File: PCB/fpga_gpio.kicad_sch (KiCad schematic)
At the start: 6 parts, among them J8 Pin header, 2x4, J9 Pin header, 2x4, U14 TPAZ1043-04F, U15 TPAZ1043-04F, U16 TPAZ1043-04F, U17 TPAZ1043-04F

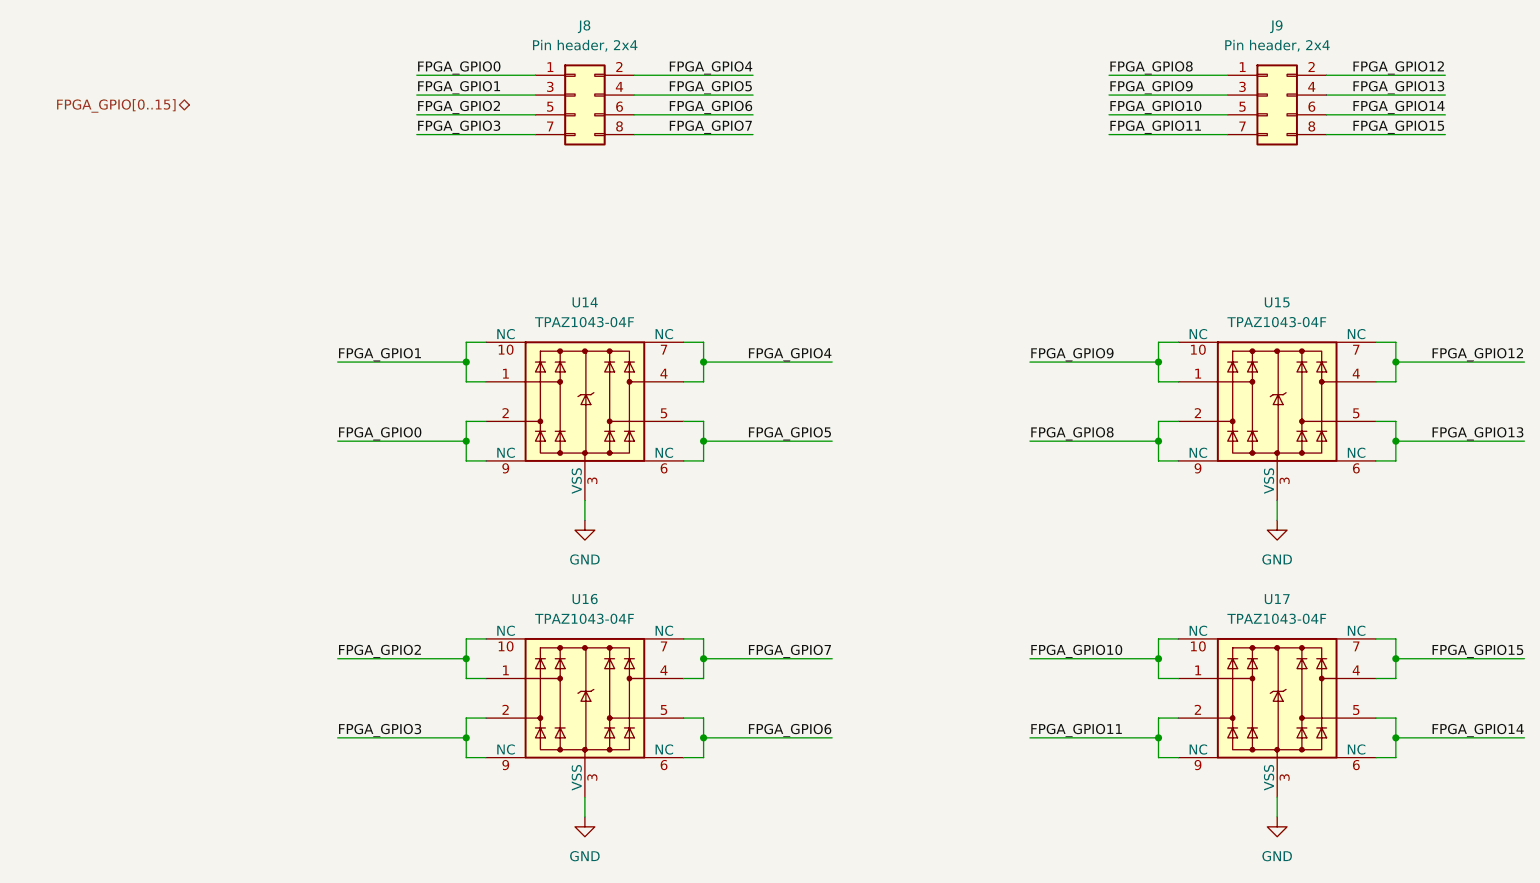
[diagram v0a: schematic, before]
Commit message: Improve the ESD protection
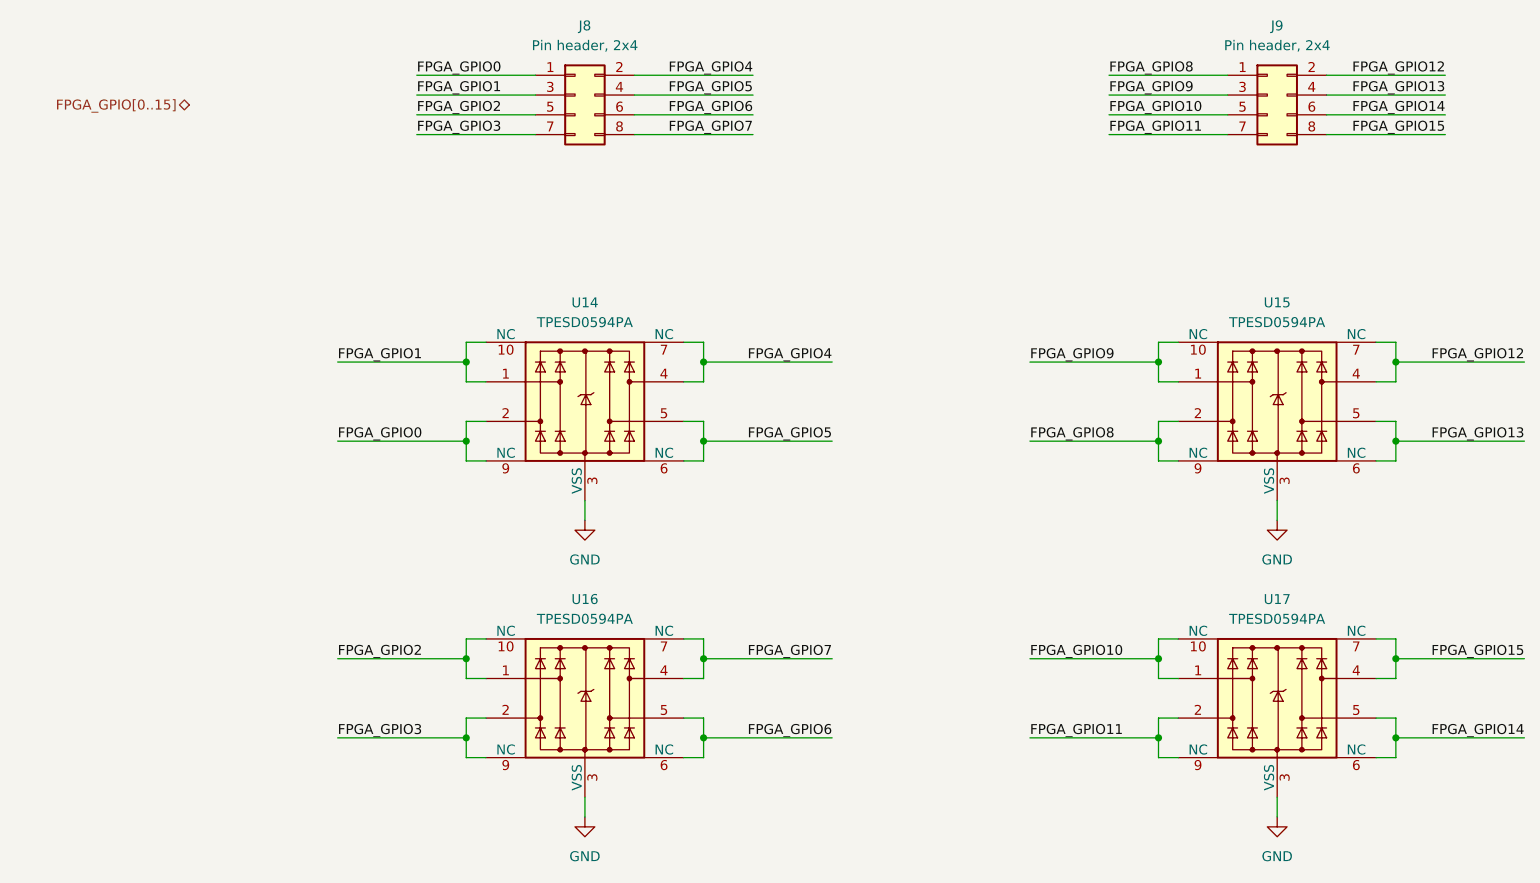
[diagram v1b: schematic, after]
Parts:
- U14, U15, U16, U17: value TPAZ1043-04F -> TPESD0594PA; LCSC C2827673 -> C42436622; Part_number TPAZ1043-04F -> TPESD0594PA
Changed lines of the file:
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@@
 		(dnp no)
 		(fields_autoplaced yes)
-		(property "Reference" "#PWR061"
+		(property "Reference" "#PWR063"
 			(at 101.6 154.94 0)
 			(effects
@@
 			(project "clavier"
 				(path "/6362c6e0-59ef-40d3-b6e0-7e9dfe7b9b20/d73938da-f0ba-48e3-aac9-a36988c25c2c/b5b36560-d80b-424a-94c9-5c93a5ca4fe2"
-					(reference "#PWR061")
+					(reference "#PWR063")
 					(unit 1)
 				)
@@
 		(dnp no)
 		(fields_autoplaced yes)
-		(property "Reference" "#PWR060"
+		(property "Reference" "#PWR062"
 			(at 190.5 116.84 0)
 			(effects
@@
 			(project "clavier"
 				(path "/6362c6e0-59ef-40d3-b6e0-7e9dfe7b9b20/d73938da-f0ba-48e3-aac9-a36988c25c2c/b5b36560-d80b-424a-94c9-5c93a5ca4fe2"
-					(reference "#PWR060")
+					(reference "#PWR062")
 					(unit 1)
 				)
@@
 		(dnp no)
 		(fields_autoplaced yes)
-		(property "Reference" "#PWR062"
+		(property "Reference" "#PWR064"
 			(at 190.5 154.94 0)
 			(effects
@@
 			(project "clavier"
 				(path "/6362c6e0-59ef-40d3-b6e0-7e9dfe7b9b20/d73938da-f0ba-48e3-aac9-a36988c25c2c/b5b36560-d80b-424a-94c9-5c93a5ca4fe2"
-					(reference "#PWR062")
+					(reference "#PWR064")
 					(unit 1)
 				)
@@
 			)
 		)
-		(property "Value" "TPAZ1043-04F"
+		(property "Value" "TPESD0594PA"
 			(at 190.5 123.19 0)
 			(effects
@@
 			)
 		)
-		(property "Datasheet" "https://www.lcsc.com/datasheet/lcsc_datasheet_2411121100_TECH-PUBLIC-TPAZ1043-04F_C2827673.pdf"
+		(property "Datasheet" "https://www.lcsc.com/datasheet/lcsc_datasheet_2501161435_TECH-PUBLIC-TPESD0594PA_C42436622.pdf"
 			(at 190.5 133.35 0)
 			(effects
@@
 			)
 		)
-		(property "LCSC" "C2827673"
+		(property "LCSC" "C42436622"
 			(at 190.5 133.35 0)
 			(effects
@@
 			)
 		)
-		(property "Part_number" "TPAZ1043-04F"
+		(property "Part_number" "TPESD0594PA"
 			(at 190.5 133.35 0)
 			(effects
@@
 			)
 		)
-		(property "Value" "TPAZ1043-04F"
+		(property "Value" "TPESD0594PA"
 			(at 190.5 85.09 0)
 			(effects
@@
 			)
 		)
-		(property "Datasheet" "https://www.lcsc.com/datasheet/lcsc_datasheet_2411121100_TECH-PUBLIC-TPAZ1043-04F_C2827673.pdf"
+		(property "Datasheet" "https://www.lcsc.com/datasheet/lcsc_datasheet_2501161435_TECH-PUBLIC-TPESD0594PA_C42436622.pdf"
 			(at 190.5 95.25 0)
 			(effects
@@
 			)
 		)
-		(property "LCSC" "C2827673"
+		(property "LCSC" "C42436622"
 			(at 190.5 95.25 0)
 			(effects
@@
 			)
 		)
-		(property "Part_number" "TPAZ1043-04F"
+		(property "Part_number" "TPESD0594PA"
 			(at 190.5 95.25 0)
 			(effects
@@
 			)
 		)
-		(property "Value" "TPAZ1043-04F"
+		(property "Value" "TPESD0594PA"
 			(at 101.6 123.19 0)
 			(effects
@@
 			)
 		)
-		(property "Datasheet" "https://www.lcsc.com/datasheet/lcsc_datasheet_2411121100_TECH-PUBLIC-TPAZ1043-04F_C2827673.pdf"
+		(property "Datasheet" "https://www.lcsc.com/datasheet/lcsc_datasheet_2501161435_TECH-PUBLIC-TPESD0594PA_C42436622.pdf"
 			(at 101.6 133.35 0)
 			(effects
@@
 			)
 		)
-		(property "LCSC" "C2827673"
+		(property "LCSC" "C42436622"
 			(at 101.6 133.35 0)
 			(effects
@@
 			)
 		)
-		(property "Part_number" "TPAZ1043-04F"
+		(property "Part_number" "TPESD0594PA"
 			(at 101.6 133.35 0)
 			(effects
@@
 			)
 		)
-		(property "Value" "TPAZ1043-04F"
+		(property "Value" "TPESD0594PA"
 			(at 101.6 85.09 0)
 			(effects
@@
 			)
 		)
-		(property "Datasheet" "https://www.lcsc.com/datasheet/lcsc_datasheet_2411121100_TECH-PUBLIC-TPAZ1043-04F_C2827673.pdf"
+		(property "Datasheet" "https://www.lcsc.com/datasheet/lcsc_datasheet_2501161435_TECH-PUBLIC-TPESD0594PA_C42436622.pdf"
 			(at 101.6 95.25 0)
 			(effects
@@
 			)
 		)
-		(property "LCSC" "C2827673"
+		(property "LCSC" "C42436622"
 			(at 101.6 95.25 0)
 			(effects
@@
 			)
 		)
-		(property "Part_number" "TPAZ1043-04F"
+		(property "Part_number" "TPESD0594PA"
 			(at 101.6 95.25 0)
 			(effects
@@
 		(dnp no)
 		(fields_autoplaced yes)
-		(property "Reference" "#PWR059"
+		(property "Reference" "#PWR061"
 			(at 101.6 116.84 0)
 			(effects
@@
 			(project "clavier"
 				(path "/6362c6e0-59ef-40d3-b6e0-7e9dfe7b9b20/d73938da-f0ba-48e3-aac9-a36988c25c2c/b5b36560-d80b-424a-94c9-5c93a5ca4fe2"
-					(reference "#PWR059")
-					(unit 1)
-				)
+					(reference "#PWR061")
+					(unit 1)
+				)

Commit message: Complete the PCB routing
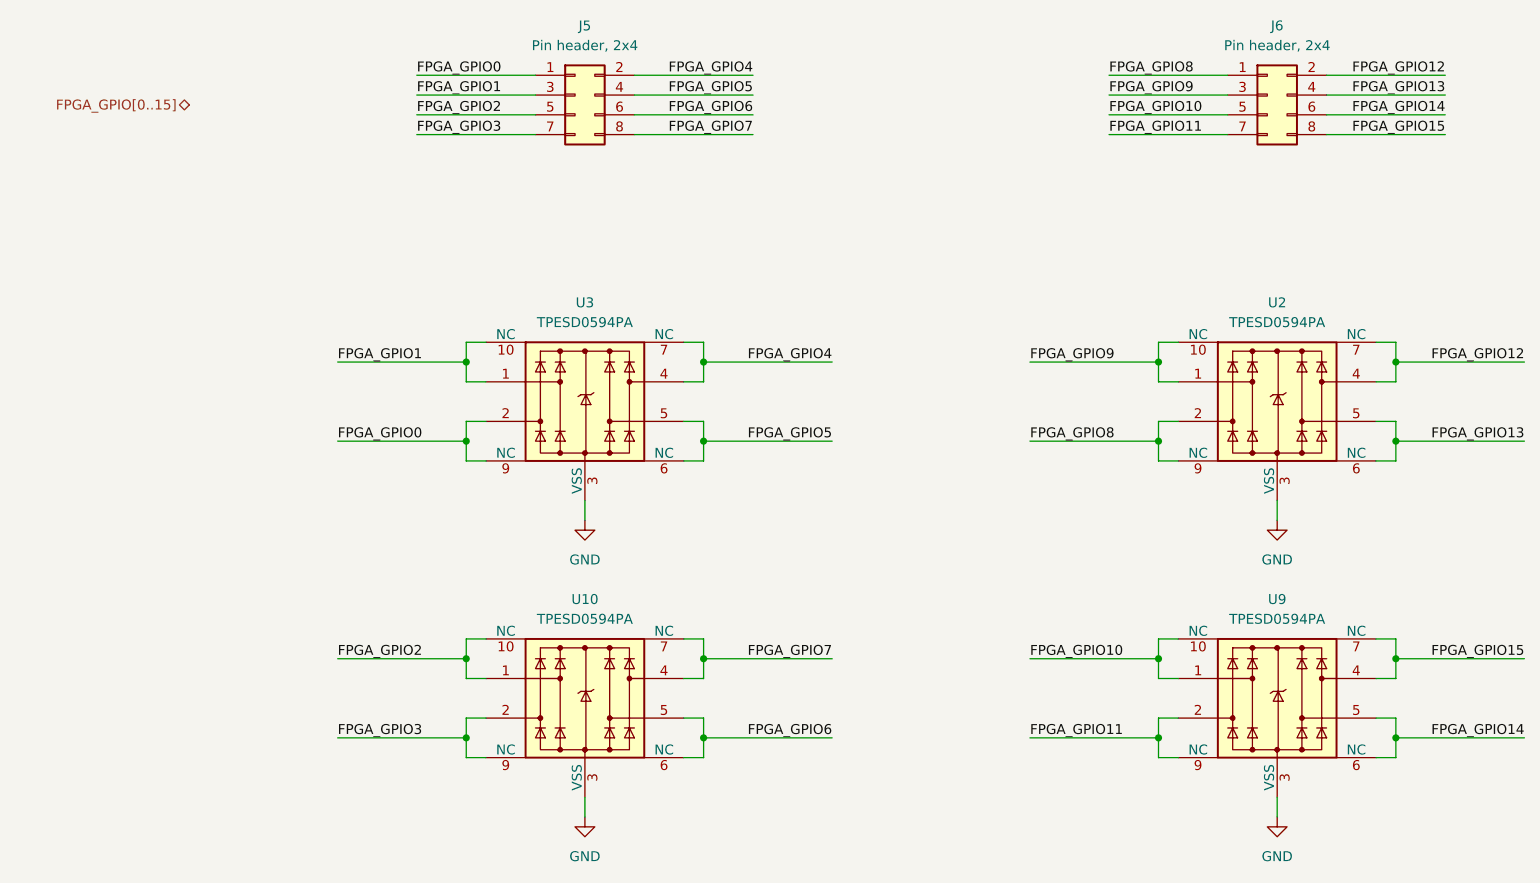
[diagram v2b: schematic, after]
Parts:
- renumbered J8 to J5, J9 to J6, U16 to U10, U15 to U2, U14 to U3, U17 to U9
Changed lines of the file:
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@@
 	(title_block
 		(title "Clavier - FPGA GPIOs")
-		(date "2025-06-21")
+		(date "2025-06-22")
 		(rev "1.0")
 		(company "Copyright (c) 2025 L. Sartory")
@@
 		(dnp no)
 		(fields_autoplaced yes)
-		(property "Reference" "J9"
+		(property "Reference" "J6"
 			(at 190.5 46.99 0)
 			(effects
@@
 			(project "clavier"
 				(path "/6362c6e0-59ef-40d3-b6e0-7e9dfe7b9b20/d73938da-f0ba-48e3-aac9-a36988c25c2c/b5b36560-d80b-424a-94c9-5c93a5ca4fe2"
-					(reference "J9")
+					(reference "J6")
 					(unit 1)
 				)
@@
 		(dnp no)
 		(fields_autoplaced yes)
-		(property "Reference" "U17"
+		(property "Reference" "U9"
 			(at 190.5 120.65 0)
 			(effects
@@
 			(project "clavier"
 				(path "/6362c6e0-59ef-40d3-b6e0-7e9dfe7b9b20/d73938da-f0ba-48e3-aac9-a36988c25c2c/b5b36560-d80b-424a-94c9-5c93a5ca4fe2"
-					(reference "U17")
+					(reference "U9")
 					(unit 1)
 				)
@@
 		(dnp no)
 		(fields_autoplaced yes)
-		(property "Reference" "U15"
+		(property "Reference" "U2"
 			(at 190.5 82.55 0)
 			(effects
@@
 			(project "clavier"
 				(path "/6362c6e0-59ef-40d3-b6e0-7e9dfe7b9b20/d73938da-f0ba-48e3-aac9-a36988c25c2c/b5b36560-d80b-424a-94c9-5c93a5ca4fe2"
-					(reference "U15")
+					(reference "U2")
 					(unit 1)
 				)
@@
 		(dnp no)
 		(fields_autoplaced yes)
-		(property "Reference" "U16"
+		(property "Reference" "U10"
 			(at 101.6 120.65 0)
 			(effects
@@
 			(project "clavier"
 				(path "/6362c6e0-59ef-40d3-b6e0-7e9dfe7b9b20/d73938da-f0ba-48e3-aac9-a36988c25c2c/b5b36560-d80b-424a-94c9-5c93a5ca4fe2"
-					(reference "U16")
+					(reference "U10")
 					(unit 1)
 				)
@@
 		(dnp no)
 		(fields_autoplaced yes)
-		(property "Reference" "U14"
+		(property "Reference" "U3"
 			(at 101.6 82.55 0)
 			(effects
@@
 			(project "clavier"
 				(path "/6362c6e0-59ef-40d3-b6e0-7e9dfe7b9b20/d73938da-f0ba-48e3-aac9-a36988c25c2c/b5b36560-d80b-424a-94c9-5c93a5ca4fe2"
-					(reference "U14")
+					(reference "U3")
 					(unit 1)
 				)
@@
 		(dnp no)
 		(fields_autoplaced yes)
-		(property "Reference" "J8"
+		(property "Reference" "J5"
 			(at 101.6 46.99 0)
 			(effects
@@
 			(project "clavier"
 				(path "/6362c6e0-59ef-40d3-b6e0-7e9dfe7b9b20/d73938da-f0ba-48e3-aac9-a36988c25c2c/b5b36560-d80b-424a-94c9-5c93a5ca4fe2"
-					(reference "J8")
+					(reference "J5")
 					(unit 1)
 				)
